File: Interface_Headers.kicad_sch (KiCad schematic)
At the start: 13 parts, among them J1 BTB_10132798-062100LF, J22 USB_C_Receptacle_USB2.0_16P, J3 SWDB, U7 USBLC6-2SC6

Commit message: Pin typo fix
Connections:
- net GND: now also U1.2; no longer U1.3
- net RST_BTN: now also U1.3; no longer U1.2
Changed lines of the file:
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@@
 	)
 	(symbol
-		(lib_name "BTN_SKSCLCE010_1")
 		(lib_id "Personal_Projects:BTN_SKSCLCE010")
 		(at 245.11 229.87 270)

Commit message: Update
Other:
- company: (none) -> Peter Hancak
- title: (none) -> STM32H7S3 Board
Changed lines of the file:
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@@
 	(generator_version "8.0")
 	(paper "A3")
+	(title_block
+		(title "STM32H7S3 Board")
+		(date "2026-03-17")
+		(rev "B")
+		(company "Peter Hancak")
+	)
 	(junction
 		(at 54.61 222.25)

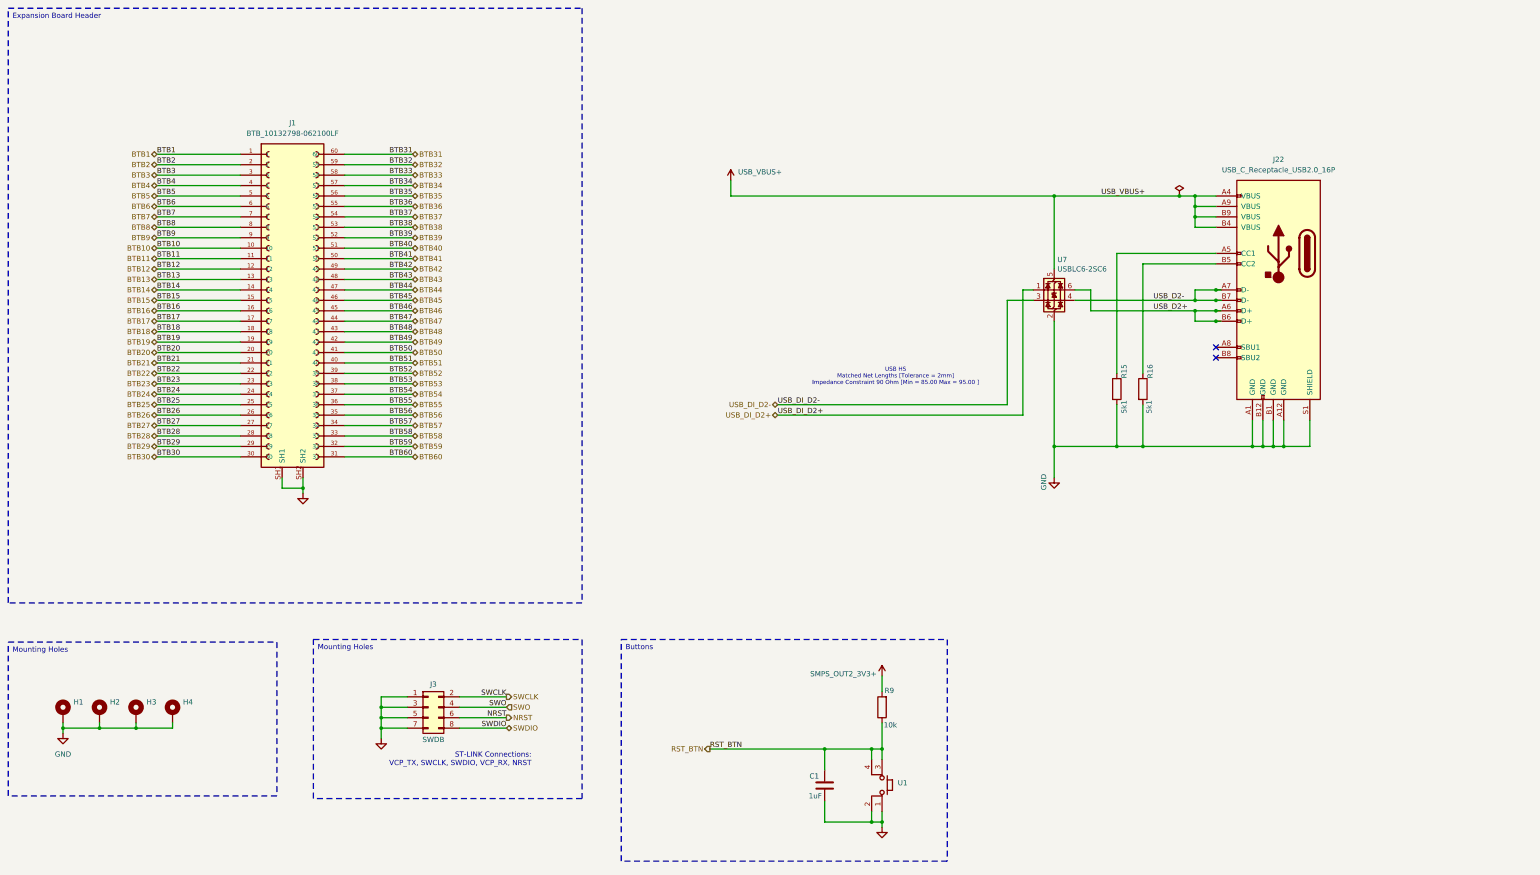
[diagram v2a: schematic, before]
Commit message: Added I2C to the LCD interface
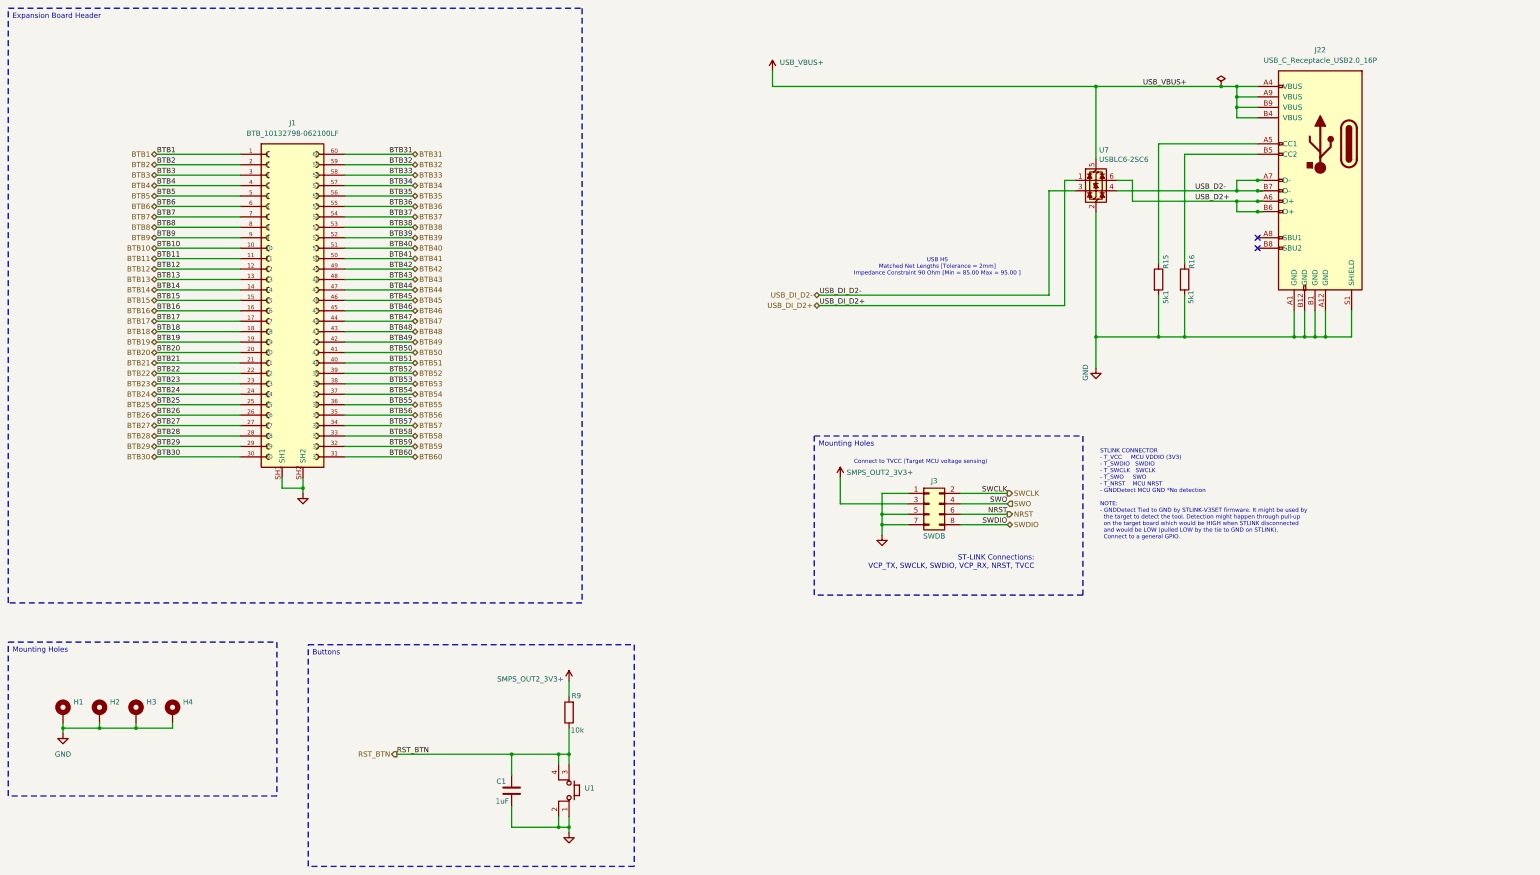
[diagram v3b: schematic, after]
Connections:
- net GND: no longer J3.3 (Pin_3)
- net SMPS_OUT2_3V3+: now also J3.3 (Pin_3)
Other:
- note added: "Connect to TVCC (Target MCU voltage sensing)"
- note added: "ST-LINK Connections: VCP_TX, SWCLK, SWDIO, VCP_RX, NRST, TVCC"
- note added: "STLINK CONNECTOR - T_VCC MCU VDDIO (3V3) - T_SWDIO SWDIO - T_SWCLK SWCLK - T_SWO SWO - T_NRST MCU NRST - GNDDetect MCU GND *No detection NOTE: - GNDDetect Tied to GND by STLINK-V3SET firmware. It might be used by the target to detect the tool. Detection might happen through pull-up on the target board which would be HIGH when STLINK disconnected and would be LOW (pulled LOW by the tie to GND on S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"
- note removed: "ST-LINK Connections: VCP_TX, SWCLK, SWDIO, VCP_RX, NRST"
- moved on the sheet: C1, J22, J3, R15, R16, R9, U1, U7

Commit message: Update
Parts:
- added R17, R18: 10k, Resistor_SMD:R_0603_1608Metric, symbol Device:R
- added R19, R22: 22R, Resistor_SMD:R_0603_1608Metric, symbol Device:R
- U1: value ~ -> (none)
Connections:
- net GND: now also R17.1
- net SMPS_OUT2_3V3+: now also R18.1
- net SWCLK: now also R19.2; no longer J3.2 (Pin_2)
- net SWDIO: now also R22.2; no longer J3.8 (Pin_8)
- new net SWCLK_R: J3.2 (Pin_2), R17.2, R19.1
- new net SWDIO_R: J3.8 (Pin_8), R18.2, R22.1
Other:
- moved on the sheet: J3
